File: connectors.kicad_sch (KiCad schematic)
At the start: 4 parts, among them J1 Conn_01x04_Pin, J2 Conn_01x04_Pin, J3 Conn_01x09_Pin, J4 Conn_02x03_Odd_Even

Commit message: Assigned footprints to components
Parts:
- J1, J2: footprint (none) -> Connector_PinHeader_2.54mm:PinHeader_1x04_P2.54mm_Vertical
- J3: footprint (none) -> Connector_PinHeader_2.54mm:PinHeader_1x09_P2.54mm_Vertical
- J4: footprint (none) -> Connector_PinHeader_2.54mm:PinHeader_2x03_P2.54mm_Vertical
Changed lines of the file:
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@@
 			)
 		)
-		(property "Footprint" ""
+		(property "Footprint" "Connector_PinHeader_2.54mm:PinHeader_1x04_P2.54mm_Vertical"
 			(at 109.22 85.09 0)
 			(effects
@@
 			)
 		)
-		(property "Footprint" ""
+		(property "Footprint" "Connector_PinHeader_2.54mm:PinHeader_2x03_P2.54mm_Vertical"
 			(at 134.62 123.19 0)
 			(effects
@@
 			)
 		)
-		(property "Footprint" ""
+		(property "Footprint" "Connector_PinHeader_2.54mm:PinHeader_1x04_P2.54mm_Vertical"
 			(at 130.81 85.09 0)
 			(effects
@@
 			)
 		)
-		(property "Footprint" ""
+		(property "Footprint" "Connector_PinHeader_2.54mm:PinHeader_1x09_P2.54mm_Vertical"
 			(at 110.49 121.92 0)
 			(effects

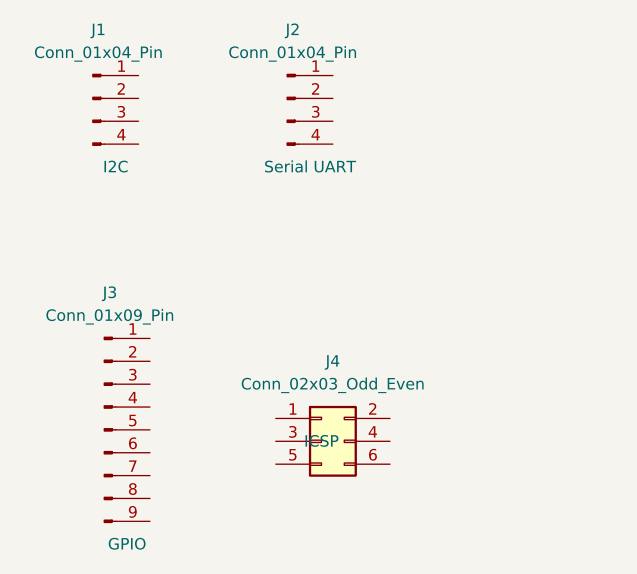
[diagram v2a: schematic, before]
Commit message: Completed wiring of second sheet + added connectection between the 2 sheets
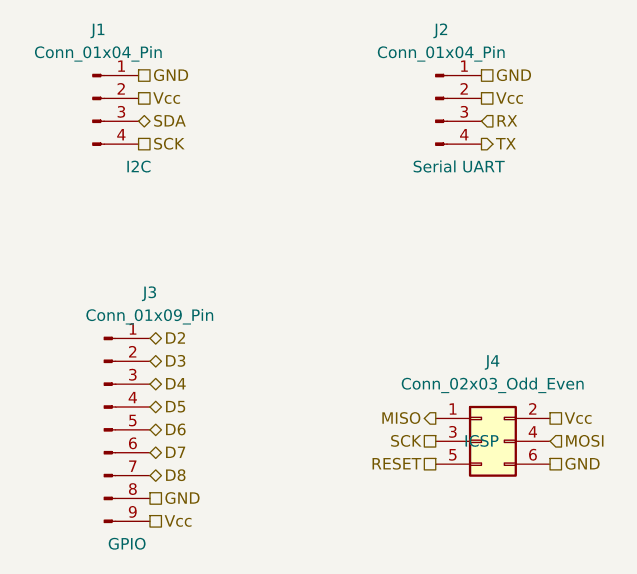
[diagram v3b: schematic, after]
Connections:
- net GND: now reaches J1.1 (Pin_1)
- net GND: now also J2.1 (Pin_1), J3.8 (Pin_8), J4.6 (Pin_6)
- net Vcc: now reaches J1.2 (Pin_2)
- net Vcc: now also J2.2 (Pin_2), J3.9 (Pin_9), J4.2 (Pin_2)
- net SDA: now reaches J1.3 (Pin_3)
- net SCK: now reaches J1.4 (Pin_4)
- net SCK: now also J4.3 (Pin_3)
- net MISO: now reaches J4.1 (Pin_1)
- net MOSI: now reaches J4.4 (Pin_4)
- net RESET: now reaches J4.5 (Pin_5)
- net RX: now reaches J2.3 (Pin_3)
- net TX: now reaches J2.4 (Pin_4)
- net D2: now reaches J3.1 (Pin_1)
- net D3: now reaches J3.2 (Pin_2)
- net D4: now reaches J3.3 (Pin_3)
- net D5: now reaches J3.4 (Pin_4)
- net D6: now reaches J3.5 (Pin_5)
- net D7: now reaches J3.6 (Pin_6)
- net D8: now reaches J3.7 (Pin_7)
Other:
- moved on the sheet: J2, J4

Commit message: Fixed 2 bugs in the Schematics diagram
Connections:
- net SCK: no longer J1.4 (Pin_4)
- new net SCL: J1.4 (Pin_4)
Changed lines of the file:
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@@
 		)
 	)
-	(hierarchical_label "SCK"
+	(hierarchical_label "SCL"
 		(shape passive)
 		(at 114.3 90.17 0)
